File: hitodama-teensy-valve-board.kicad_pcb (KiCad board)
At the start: 2 copper layers, 127 x 101.6 mm, 10 parts, among them J1 Conn_01x21_Female

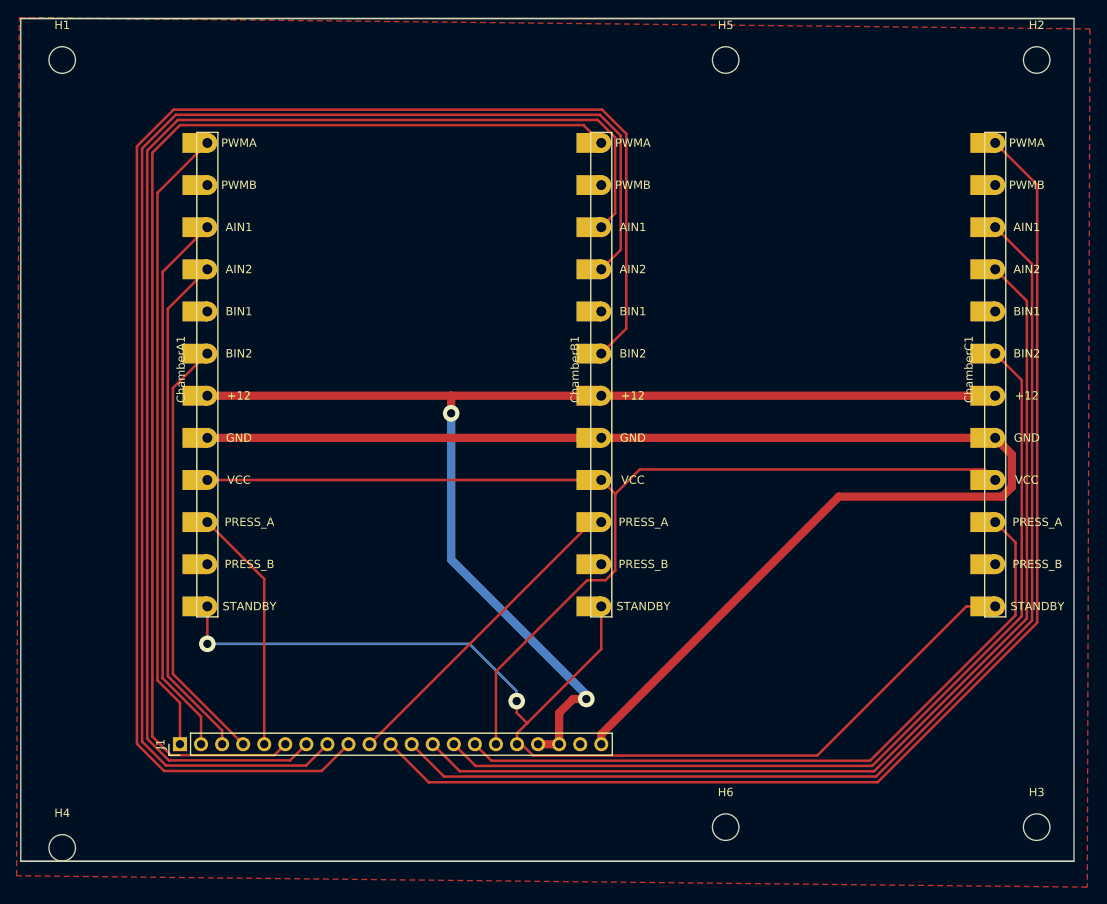
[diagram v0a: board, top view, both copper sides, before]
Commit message: fixed forgotten swap of pin headers on teensy-valves-board bridge
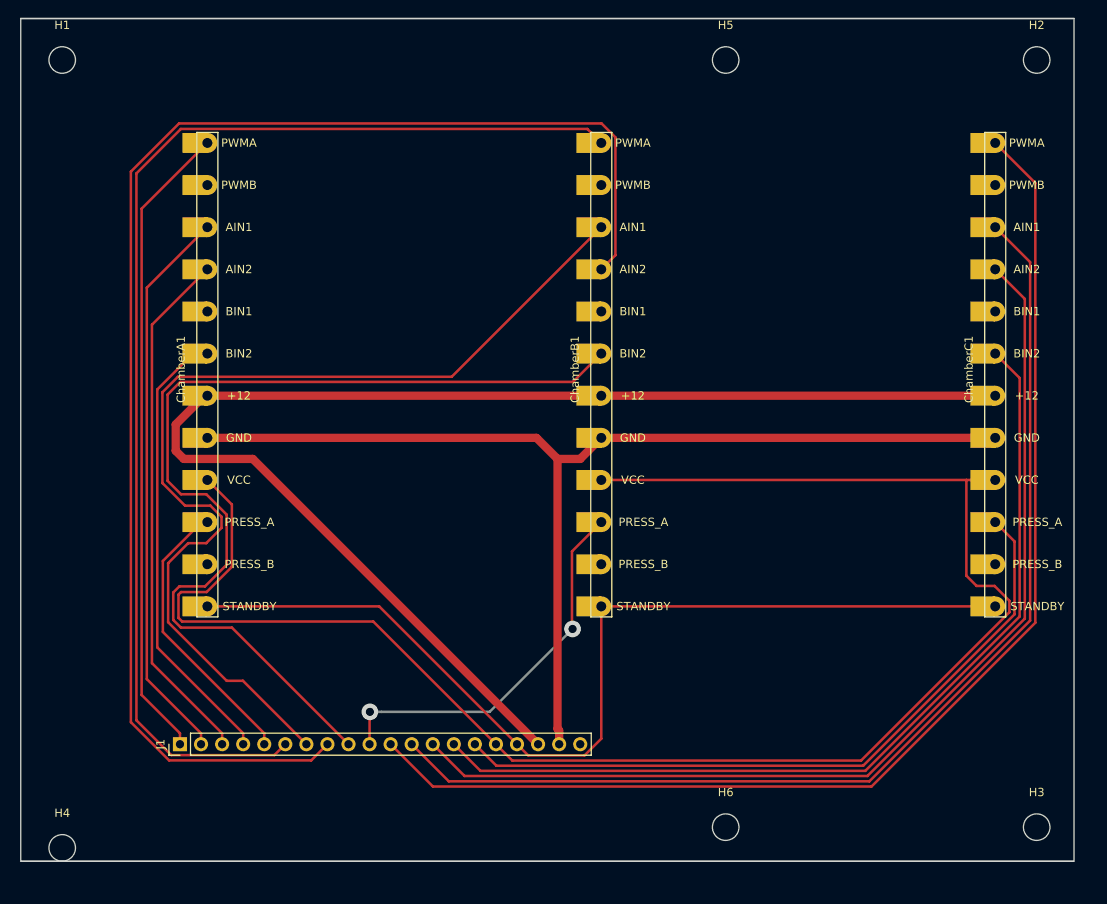
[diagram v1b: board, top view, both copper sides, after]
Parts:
- J1: value Conn_01x21_Female -> Conn_01x20_Female; footprint Connector_PinHeader_2.54mm:PinHeader_1x21_P2.54mm_Vertical -> Connector_PinHeader_2.54mm:PinHeader_1x20_P2.54mm_Vertical
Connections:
- J1 pad 19: +12V -> GND
- J1 pad 20: GND -> Net-(J1-Pad20)
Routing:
- net /ChamberB.D3: track 190.0 -> 118.1 mm
- net VCC: track 134.9 -> 203.9 mm
- net /ChamberB.D1: track 162.3 -> 120.3 mm
- net GND: track 164.8 -> 131.6 mm
- net /All.Stby: track 135.3 -> 119.2 mm, vias 2 -> 0
- net +12V: track 148.6 -> 161.8 mm, vias 2 -> 0
- net /ChamberB.ADC: track 39.0 -> 46.9 mm, vias 0 -> 2
- net /ChamberA.ADC: track 29.6 -> 34.5 mm
- net /ChamberB.D2: track 173.7 -> 170.9 mm
- net /ChamberA.D3: track 52.3 -> 54.9 mm
- net /ChamberA.PWM: track 76.1 -> 77.7 mm
- net /ChamberA.D1: track 66.5 -> 68.1 mm
- net /ChamberA.D2: track 61.9 -> 63.5 mm
- net /ChamberB.PWM: track 144.3 -> 145.2 mm
- removed copper zone on F.Cu, net GND

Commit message: 2 row connector, routed on intermediate board
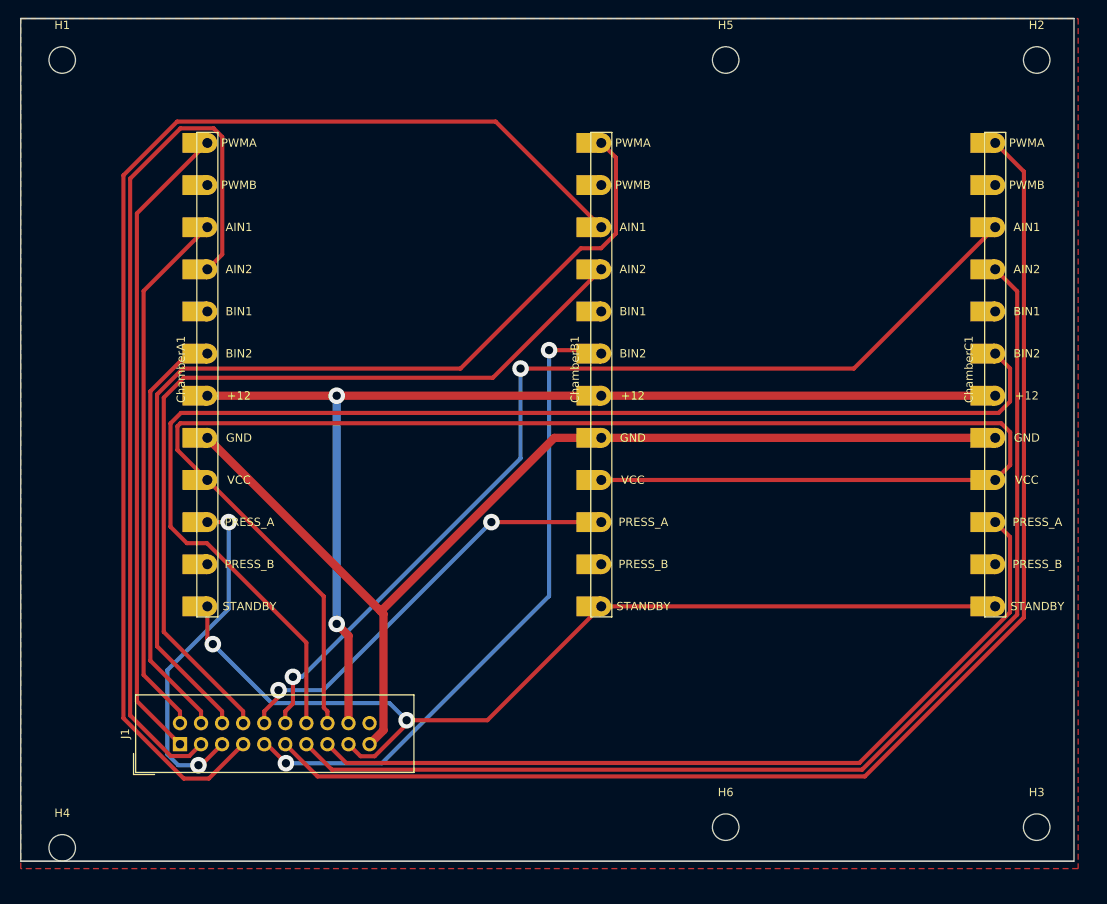
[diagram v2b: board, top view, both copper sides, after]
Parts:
- J1: footprint Connector_PinHeader_2.54mm:PinHeader_1x20_P2.54mm_Vertical -> Connector_IDC:IDC-Header_2x10_P2.54mm_Vertical
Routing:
- net /ChamberB.D2: track 170.9 -> 102.4 mm
- net /ChamberA.D2: track 63.5 -> 106.6 mm
- net /ChamberC.D3: track 110.2 -> 153.2 mm
- net /ChamberB.D3: track 118.1 -> 79.8 mm, vias 0 -> 2
- net /ChamberB.D1: track 120.3 -> 150.2 mm
- net /ChamberB.PWM: track 145.2 -> 117.9 mm
- net +12V: track 161.8 -> 135.1 mm, vias 0 -> 2
- net /ChamberC.ADC: track 85.8 -> 102.4 mm
- net /ChamberC.D1: track 133.6 -> 119.4 mm, vias 0 -> 2
- net /ChamberC.D2: track 124.4 -> 137.5 mm
- net /ChamberC.PWM: track 147.9 -> 157.3 mm
- net /ChamberA.ADC: track 34.5 -> 41.8 mm, vias 0 -> 2
- net VCC: track 203.9 -> 198.3 mm
- net /ChamberB.ADC: track 46.9 -> 52.0 mm
- net /ChamberA.D3: track 54.9 -> 51.3 mm
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- added copper zone on F.Cu, net GND
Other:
- net class Default: trace_width 0.31 -> 0.5

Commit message: even greater trace widths
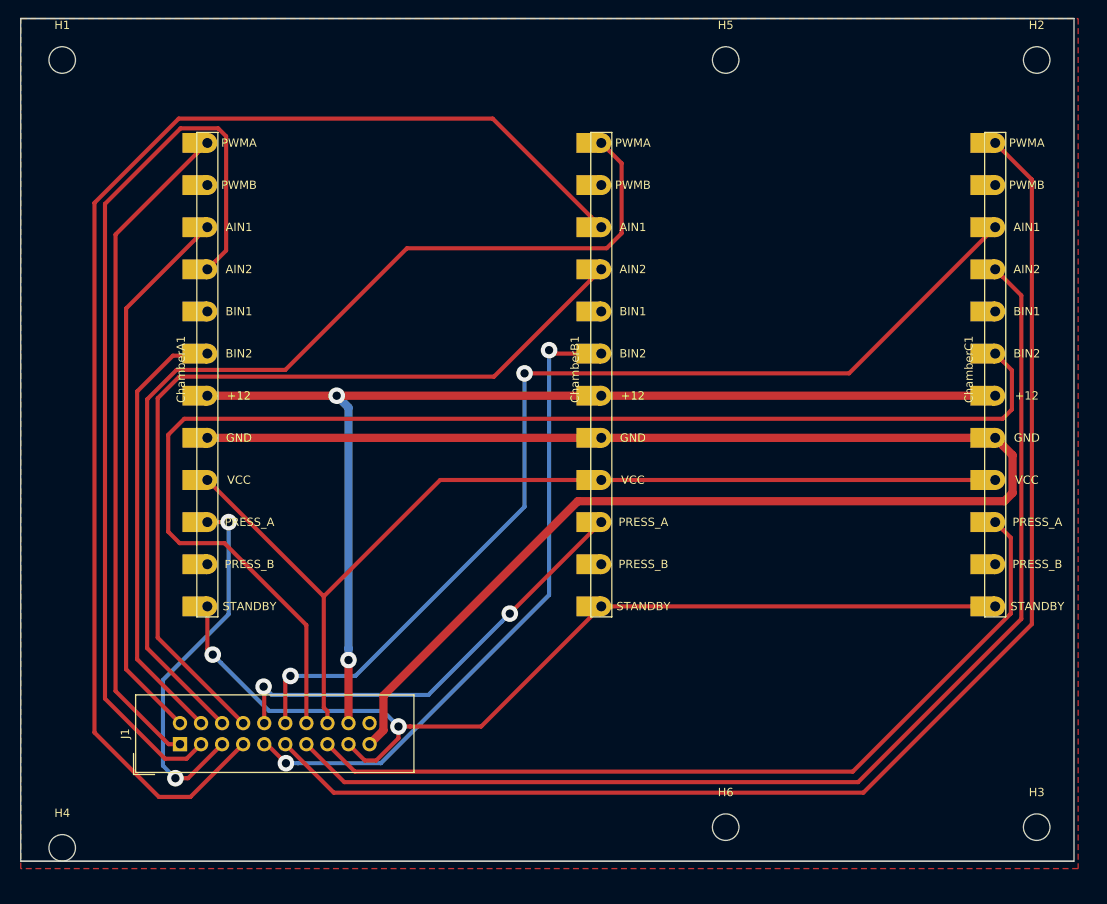
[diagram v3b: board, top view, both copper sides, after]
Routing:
- net VCC: track 198.3 -> 122.1 mm
- net GND: track 129.2 -> 195.0 mm
- net /ChamberB.D1: track 150.2 -> 158.4 mm
- net /ChamberA.D2: track 106.6 -> 110.7 mm
- net /ChamberC.PWM: track 157.3 -> 160.7 mm
- net /ChamberC.D1: track 119.4 -> 122.8 mm
- net /ChamberA.PWM: track 78.2 -> 81.1 mm
- net /ChamberA.ADC: track 41.8 -> 44.7 mm
- net /ChamberB.PWM: track 117.9 -> 120.2 mm
- net /ChamberC.D2: track 137.5 -> 139.7 mm
- net /ChamberA.D3: track 51.3 -> 53.5 mm
- net /ChamberC.D3: track 153.2 -> 155.4 mm
- net /ChamberB.ADC: track 52.0 -> 54.2 mm
- net /ChamberA.D1: track 64.8 -> 66.6 mm
- net /ChamberC.ADC: track 102.4 -> 103.5 mm
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
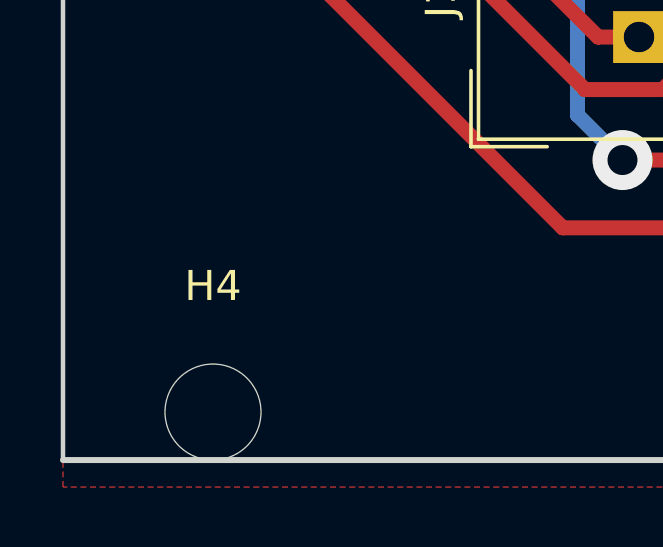
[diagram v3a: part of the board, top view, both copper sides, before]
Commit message: fix misaligned hole
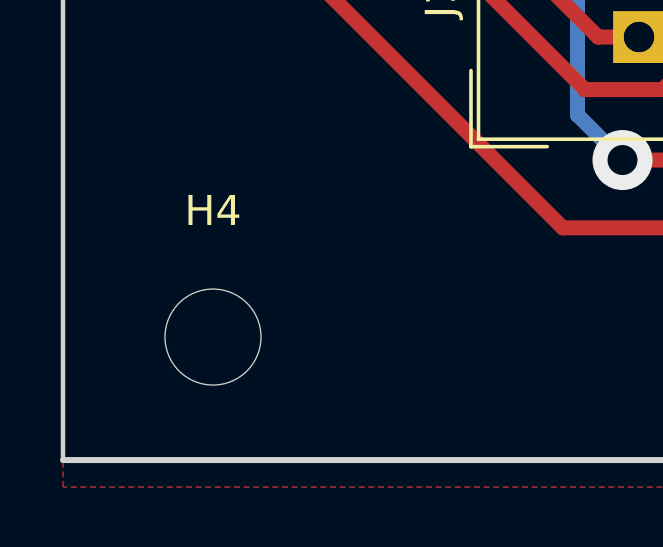
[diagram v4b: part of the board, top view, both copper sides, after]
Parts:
- moved H4 2.50 mm to (5.00, 97.5)
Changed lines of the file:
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@@
     (mod_text_size 0.000001 0.000001)
     (mod_text_width 0.15)
-    (pad_size 1.4 1.4)
-    (pad_drill 0.6)
+    (pad_size 3.2 3.2)
+    (pad_drill 3.2)
     (pad_to_mask_clearance 0.051)
     (solder_mask_min_width 0.25)
@@
   )
   (module MountingHole:MountingHole_3.2mm_M3 (layer F.Cu)
-    (at 5 100)
+    (at 5 97.5)
     (descr "Mounting Hole 3.2mm, no annular, M3")
     (tags "mounting hole 3.2mm no annular m3")

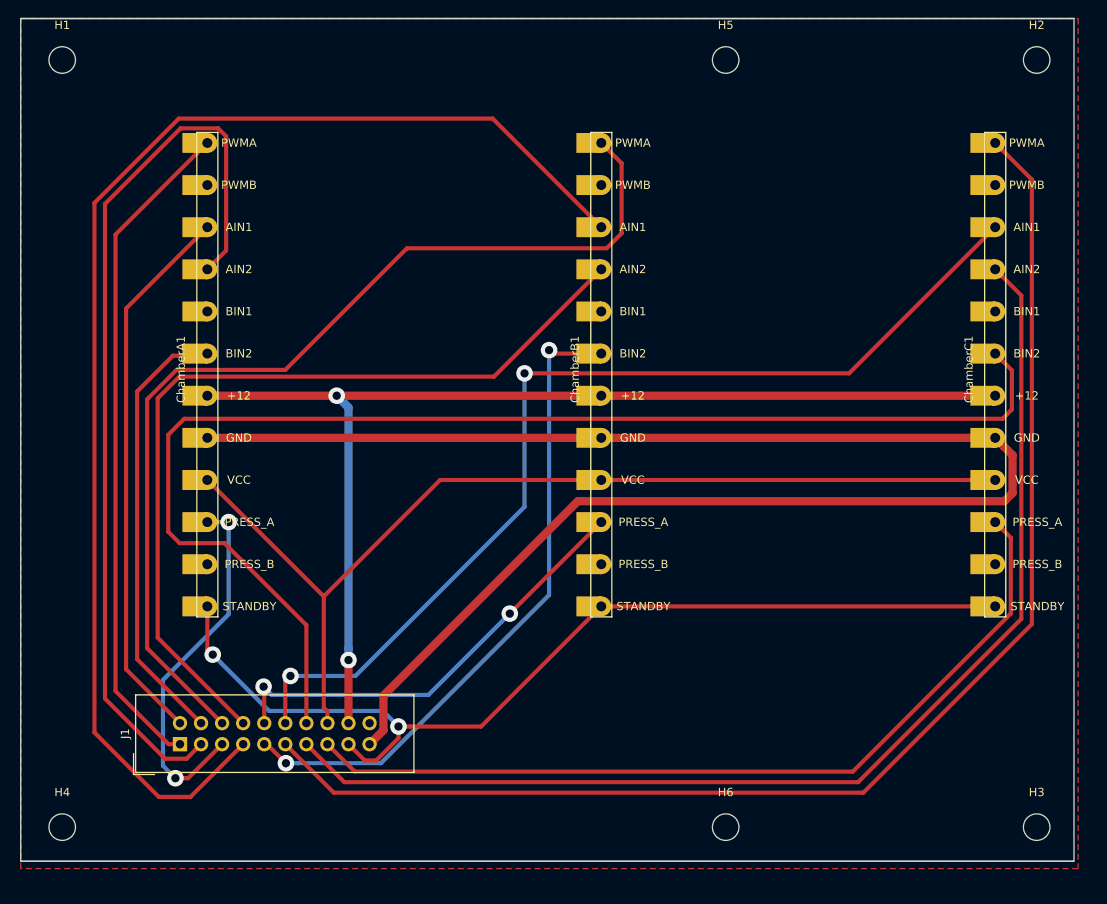
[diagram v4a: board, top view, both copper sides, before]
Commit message: change connectors into edge connector 5-5530843-3, TE Connectivity
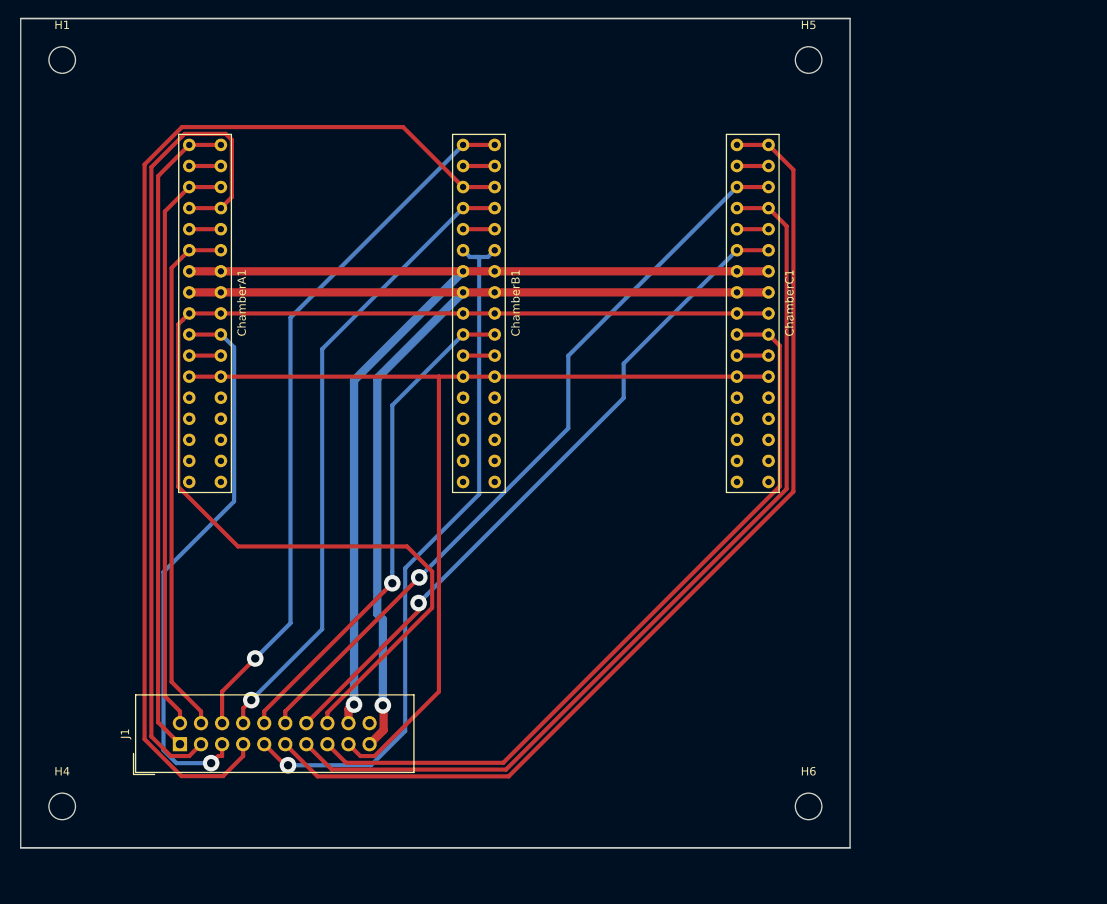
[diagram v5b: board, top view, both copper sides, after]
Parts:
- removed H2, H3: MountingHole, MountingHole:MountingHole_3.2mm_M3
- ChamberA1, ChamberB1, ChamberC1: footprint chamber_board_holder:chamber_board_holder -> chamber_board_holder:5-5530843-3 female
- moved ChamberC1 27.3 mm to (90.2, 15.2), turned to 270 degrees
- moved ChamberB1 12.9 mm to (57.1, 15.2), turned to 270 degrees
- moved H6 10.3 mm to (95.0, 95.0)
- moved H5 10.0 mm to (95.0, 5.00)
- moved H4 2.50 mm to (5.00, 95.0)
- moved ChamberA1 1.65 mm to (24.1, 15.2), turned to 270 degrees
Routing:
- net /ChamberC.D3: track 155.4 -> 82.3 mm, vias 0 -> 1
- net GND: track 195.0 -> 129.6 mm, vias 0 -> 1
- net /ChamberC.PWM: track 160.7 -> 124.0 mm
- net /ChamberB.PWM: track 120.2 -> 85.6 mm, vias 0 -> 1
- net /ChamberC.D1: track 122.8 -> 91.0 mm, vias 2 -> 1
- net /ChamberC.D2: track 139.7 -> 111.8 mm
- net VCC: track 122.1 -> 149.6 mm
- net /ChamberB.D2: track 103.4 -> 76.9 mm, vias 0 -> 1
- net /ChamberB.D1: track 158.4 -> 132.6 mm
- net /ChamberA.ADC: track 44.7 -> 67.7 mm, vias 2 -> 1
- net /ChamberC.ADC: track 103.5 -> 92.0 mm
- net /ChamberA.D2: track 110.7 -> 100.5 mm
- net /ChamberA.D3: track 53.5 -> 63.2 mm
- net /ChamberB.ADC: track 54.2 -> 60.6 mm, vias 2 -> 1
- net /ChamberB.D3: track 79.7 -> 85.7 mm, vias 2 -> 1
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- removed copper zone on F.Cu, net GND
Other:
- board size 127 x 101.6 mm -> 100 x 100 mm

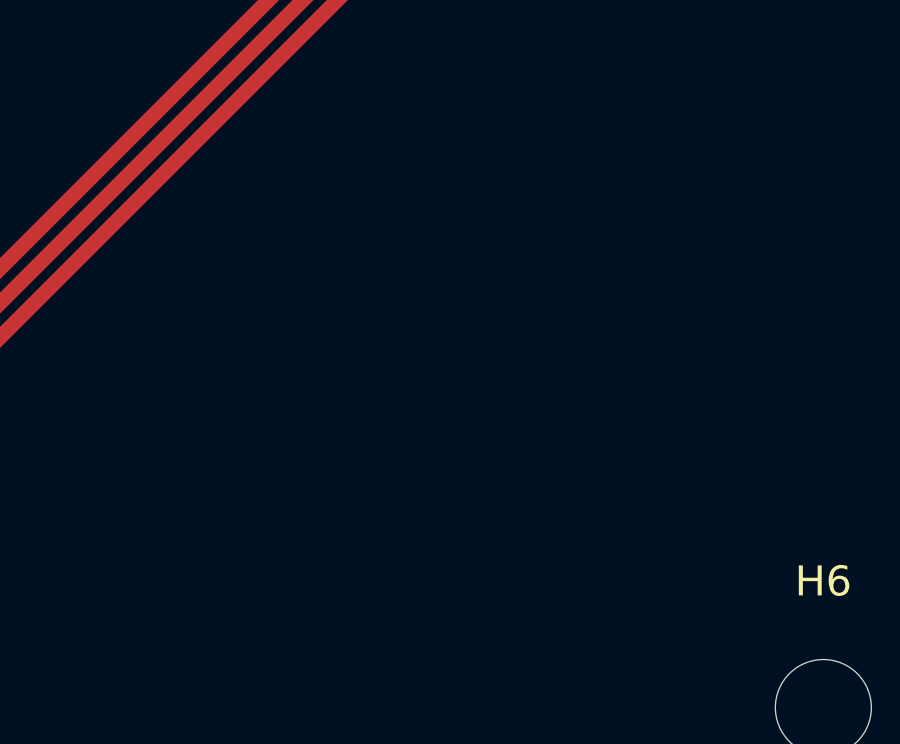
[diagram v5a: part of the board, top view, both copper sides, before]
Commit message: added logos
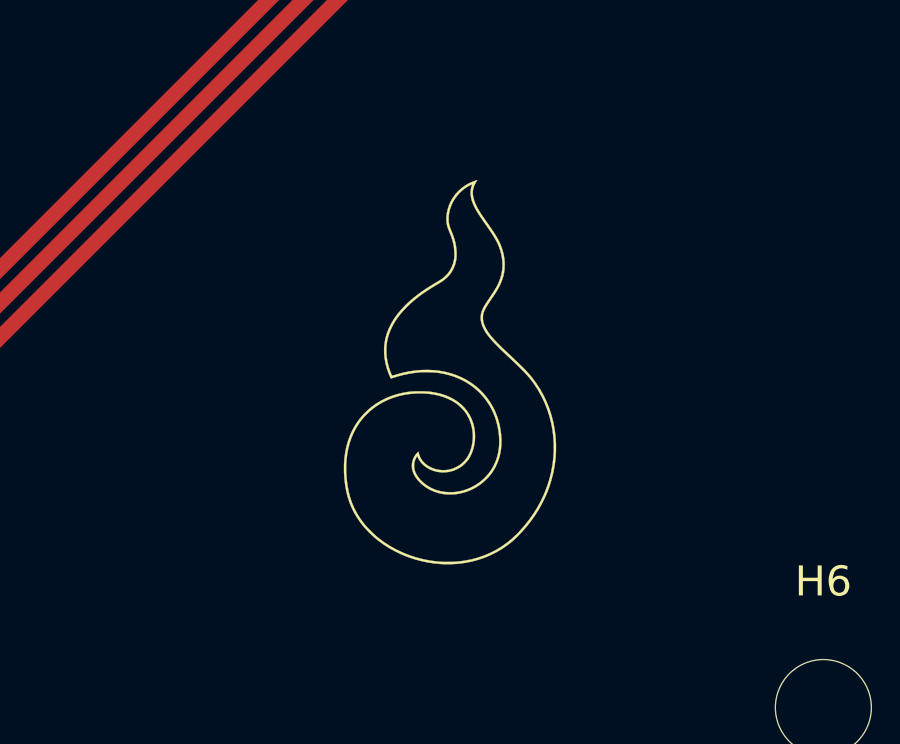
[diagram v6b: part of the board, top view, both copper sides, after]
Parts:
- added G***: LOGO, Hitodama_Logo:hitodama_vertical, F.Cu at (82.5, 83.8)
